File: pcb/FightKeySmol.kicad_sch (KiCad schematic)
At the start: 31 parts, among them J1 Conn_01x08_Male, J2 Conn_01x08_Male, U1 Pico

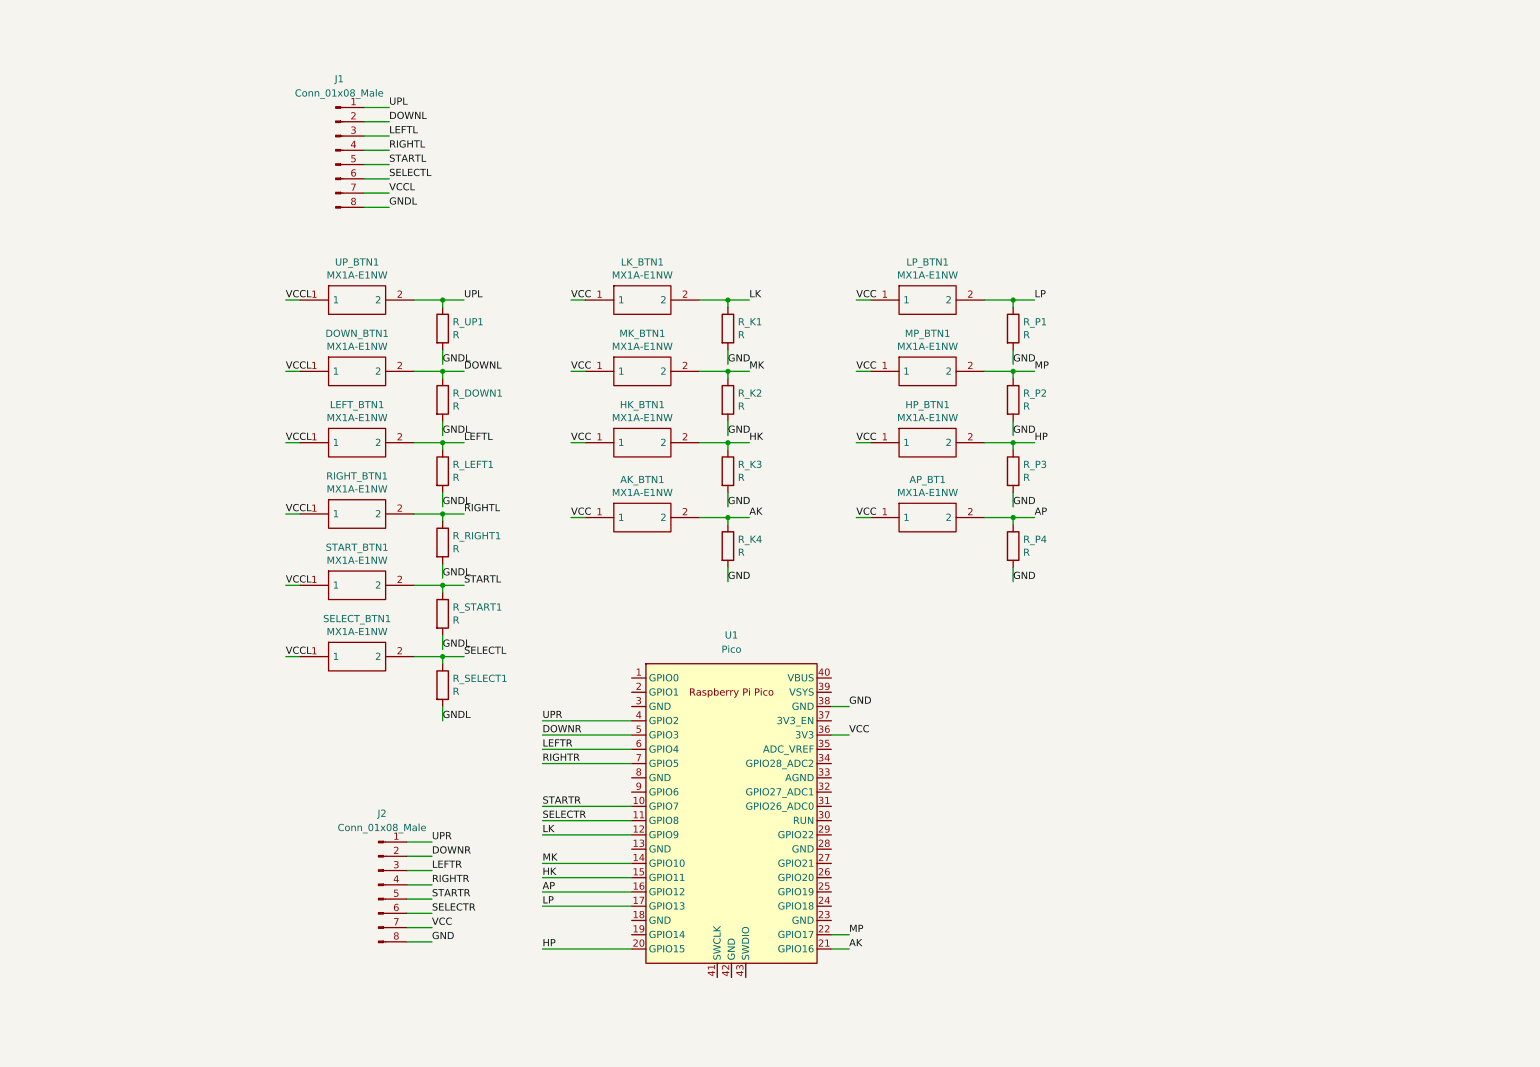
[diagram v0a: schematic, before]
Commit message: kicad_sch: redesigned to use input_pullup
This is the standard for GP2040 style sticks.
Use PICO_BOARD_CONFIG_H_

Signed-off-by: Dylan Turner <dylantdmt@gmail.com>
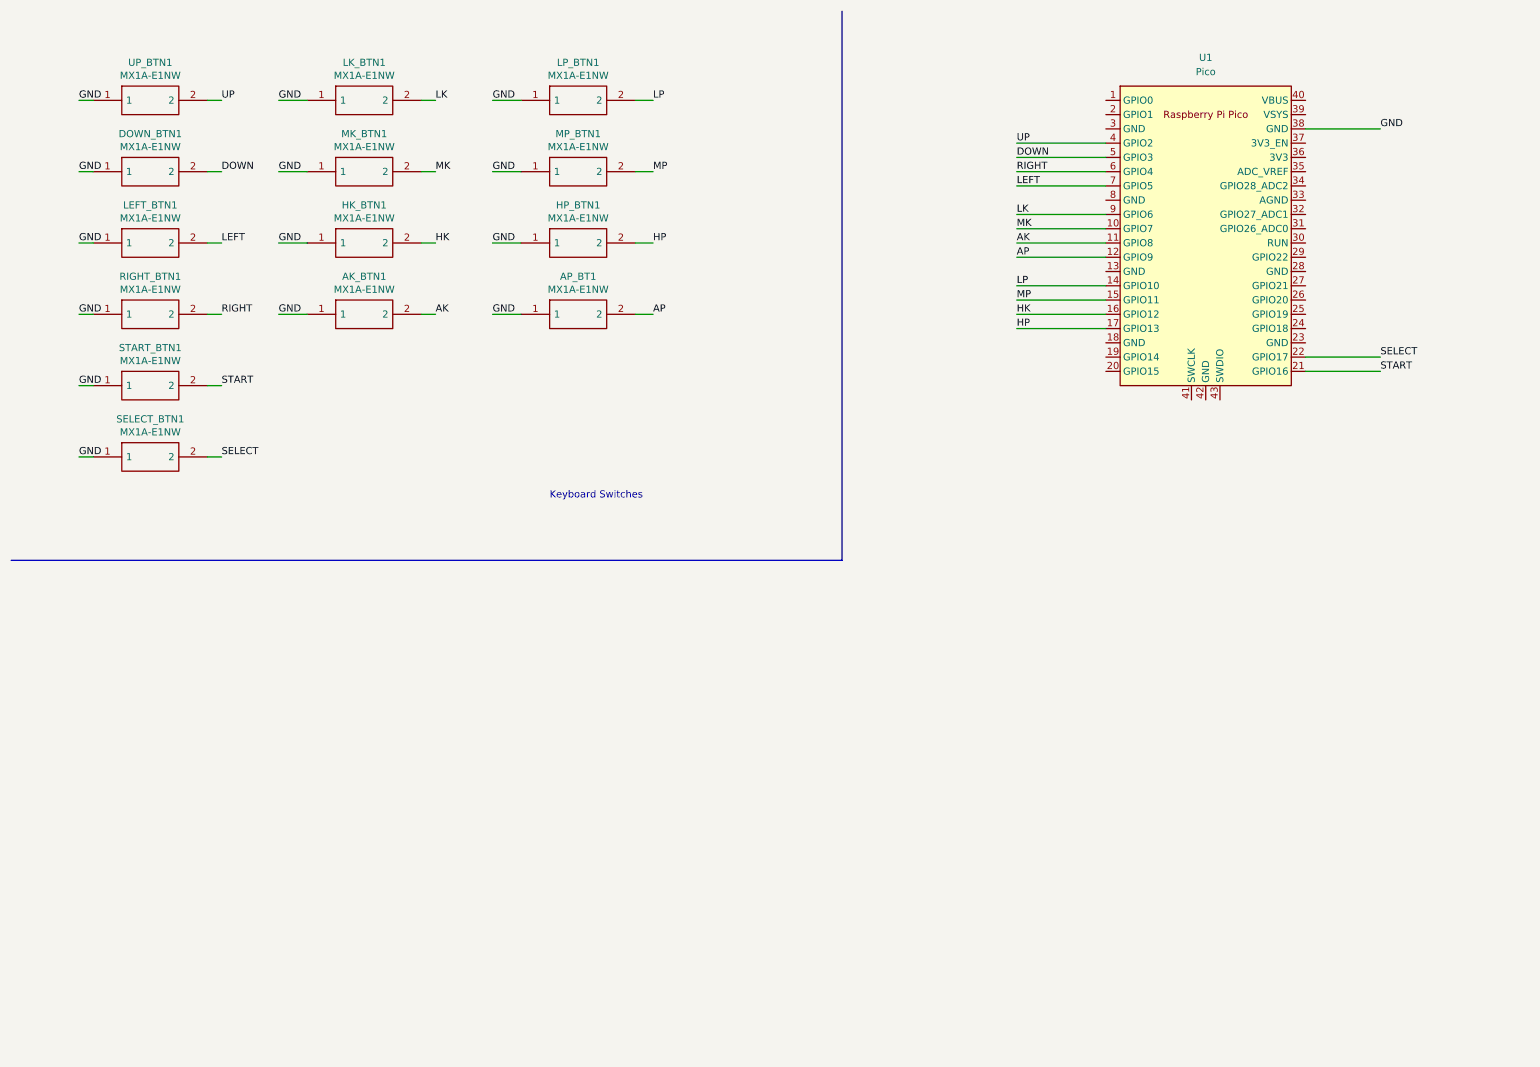
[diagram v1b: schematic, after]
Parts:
- removed J1, J2: Conn_01x08_Male, Connector_PinHeader_2.54mm:PinHeader_1x08_P2.54mm_Vertical, symbol Connector:Conn_01x08_Male
- removed R_DOWN1, R_K1, R_K2, R_K3, R_K4, R_LEFT1, R_P1, R_P2, R_P3, R_P4, R_RIGHT1, R_SELECT1, R_START1, R_UP1: R, Resistor_THT:R_Axial_DIN0204_L3.6mm_D1.6mm_P2.54mm_Vertical, symbol Device:R
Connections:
- net DOWNR is gone; now on net DOWN: U1.5 (GPIO3)
- net RIGHTL is gone; now on net RIGHT: RIGHT_BTN1.2
- net RIGHTR is gone; now on net LEFT: U1.7 (GPIO5)
- net SELECTR is gone; now on net AK: U1.11 (GPIO8)
- net STARTR is gone; now on net MK: U1.10 (GPIO7)
- net UPR is gone; now on net UP: U1.4 (GPIO2)
- net VCCL is gone; now on net GND: DOWN_BTN1.1, LEFT_BTN1.1, RIGHT_BTN1.1, SELECT_BTN1.1, START_BTN1.1, UP_BTN1.1
- net AK: no longer U1.21 (GPIO16)
- net AP: now also U1.12 (GPIO9); no longer U1.16 (GPIO12)
- net GND: now also AK_BTN1.1, AP_BT1.1, HK_BTN1.1, HP_BTN1.1, LK_BTN1.1, LP_BTN1.1, MK_BTN1.1, MP_BTN1.1
- net HK: now also U1.16 (GPIO12); no longer U1.15 (GPIO11)
- net HP: now also U1.17 (GPIO13); no longer U1.20 (GPIO15)
- net LK: now also U1.9 (GPIO6); no longer U1.12 (GPIO9)
- net LP: now also U1.14 (GPIO10); no longer U1.17 (GPIO13)
- net MK: no longer U1.14 (GPIO10)
- net MP: now also U1.15 (GPIO11); no longer U1.22 (GPIO17)
- net DOWNL renamed DOWN
- net LEFTL renamed LEFT
- net LEFTR renamed RIGHT
- net SELECTL renamed SELECT
- net SELECT: now also U1.22 (GPIO17)
- net STARTL renamed START
- net START: now also U1.21 (GPIO16)
- net UPL renamed UP
- removed net VCC: AK_BTN1.1, AP_BT1.1, HK_BTN1.1, HP_BTN1.1, LK_BTN1.1, LP_BTN1.1, MK_BTN1.1, MP_BTN1.1, U1.36 (3V3)
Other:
- note added: "Keyboard Switches"
- moved on the sheet: AK_BTN1, AP_BT1, DOWN_BTN1, HK_BTN1, HP_BTN1, LEFT_BTN1, LK_BTN1, LP_BTN1, MK_BTN1, MP_BTN1, RIGHT_BTN1, SELECT_BTN1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

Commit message: kicad_sch: added second ground on other side
Signed-off-by: Dylan Turner <dylantdmt@gmail.com>
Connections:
- net GND: now also U1.3 (GND)
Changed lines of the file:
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@@
+    (stroke (width 0) (type default) (color 0 0 0 0))
+  )
+  (wire (pts (xy 191.135 33.02) (xy 207.01 33.02))
     (stroke (width 0) (type default) (color 0 0 0 0))
   )
@@
     (effects (font (size 1.27 1.27)) (justify left bottom))
   )
+  (label "GND" (at 191.135 33.02 0)
+    (effects (font (size 1.27 1.27)) (justify left bottom))
+  )

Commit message: kicad_sch: switch start/sel
Signed-off-by: Dylan Turner <dylantdmt@gmail.com>
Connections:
- net SELECT: now also U1.21 (GPIO16); no longer U1.22 (GPIO17)
- net START: now also U1.22 (GPIO17); no longer U1.21 (GPIO16)
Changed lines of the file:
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@@
-    (effects (font (size 1.27 1.27)) (justify left bottom))
-  )
-  (label "SELECT" (at 255.905 73.66 0)
     (effects (font (size 1.27 1.27)) (justify left bottom))
   )
@@
   )
   (label "GND" (at 97.79 40.64 0)
+    (effects (font (size 1.27 1.27)) (justify left bottom))
+  )
+  (label "SELECT" (at 255.905 76.2 0)
     (effects (font (size 1.27 1.27)) (justify left bottom))
   )
@@
     (effects (font (size 1.27 1.27)) (justify left bottom))
   )
-  (label "START" (at 255.905 76.2 0)
-    (effects (font (size 1.27 1.27)) (justify left bottom))
-  )
   (label "UP" (at 49.53 27.94 0)
     (effects (font (size 1.27 1.27)) (justify left bottom))
@@
     (effects (font (size 1.27 1.27)) (justify left bottom))
   )
+  (label "START" (at 255.905 73.66 0)
+    (effects (font (size 1.27 1.27)) (justify left bottom))
+  )

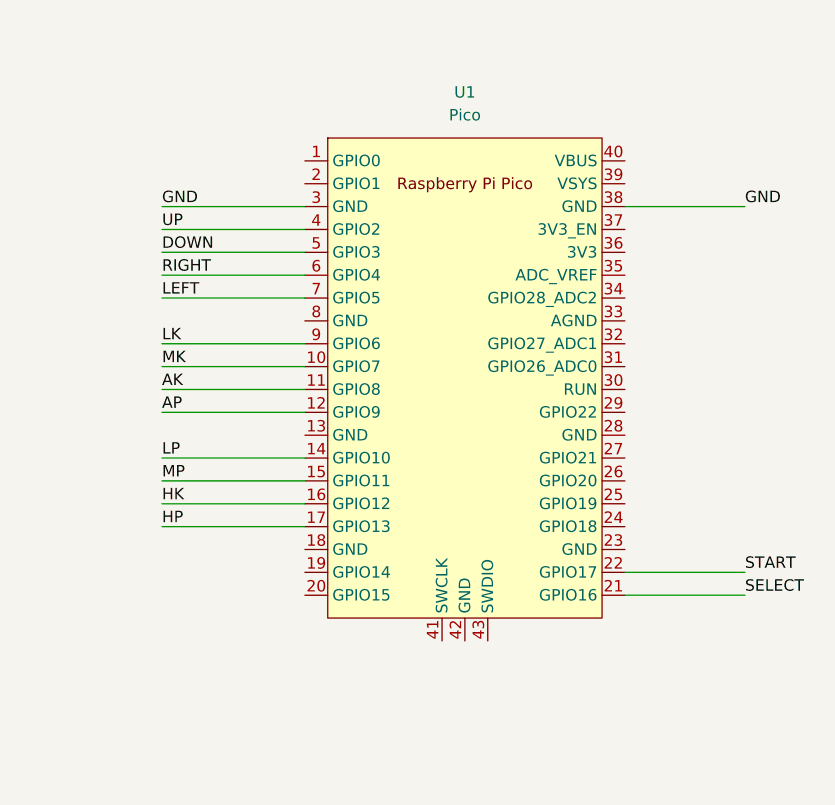
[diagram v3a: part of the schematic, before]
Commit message: kicad_sch: delete pico
Signed-off-by: Dylan Turner <dylantdmt@gmail.com>
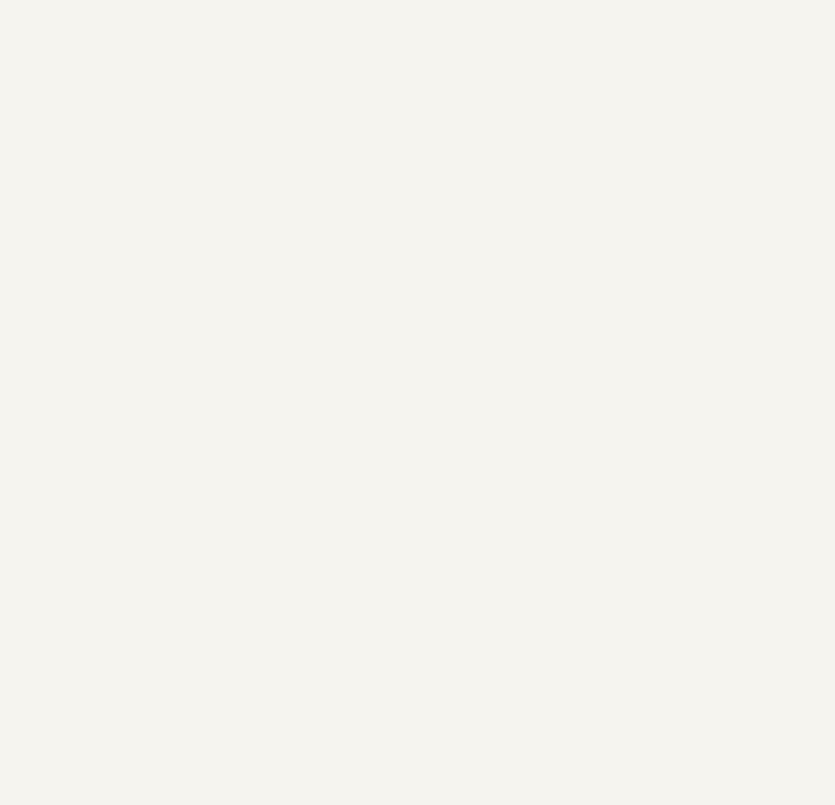
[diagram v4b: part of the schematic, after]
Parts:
- removed U1: Pico, MCU_RaspberryPi_and_Boards:RPi_Pico_SMD_TH, symbol MCU_RaspberryPi_and_Boards:Pico
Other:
- title: Fight Key PCB -> Fight Key Smol PCB
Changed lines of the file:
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@@
   (paper "A4")
   (title_block
-    (title "Fight Key PCB")
-    (date "2022-05-21")
+    (title "Fight Key Smol PCB")
+    (date "2023-04-14")
     (rev "2")
     (company "Dylan Turner")
@@
     (stroke (width 0) (type default) (color 0 0 0 0))
   )
-  (wire (pts (xy 191.135 68.58) (xy 207.01 68.58))
-    (stroke (width 0) (type default) (color 0 0 0 0))
-  )
   (wire (pts (xy 46.99 53.34) (xy 49.53 53.34))
     (stroke (width 0) (type default) (color 0 0 0 0))
   )
-  (wire (pts (xy 191.135 43.18) (xy 207.01 43.18))
-    (stroke (width 0) (type default) (color 0 0 0 0))
-  )
   (wire (pts (xy 26.67 91.44) (xy 24.13 91.44))
     (stroke (width 0) (type default) (color 0 0 0 0))
@@
     (stroke (width 0) (type default) (color 0 0 0 0))
   )
-  (wire (pts (xy 242.57 73.66) (xy 255.905 73.66))
-    (stroke (width 0) (type default) (color 0 0 0 0))
-  )
-  (wire (pts (xy 191.135 55.88) (xy 207.01 55.88))
-    (stroke (width 0) (type default) (color 0 0 0 0))
-  )
-  (wire (pts (xy 191.135 33.02) (xy 207.01 33.02))
-    (stroke (width 0) (type default) (color 0 0 0 0))
-  )
-  (wire (pts (xy 191.135 38.1) (xy 207.01 38.1))
-    (stroke (width 0) (type default) (color 0 0 0 0))
-  )
   (wire (pts (xy 85.09 66.04) (xy 87.63 66.04))
     (stroke (width 0) (type default) (color 0 0 0 0))
@@
     (stroke (width 0) (type default) (color 0 0 0 0))
   )
-  (wire (pts (xy 242.57 33.02) (xy 255.905 33.02))
-    (stroke (width 0) (type default) (color 0 0 0 0))
-  )
   (wire (pts (xy 26.67 40.64) (xy 24.13 40.64))
     (stroke (width 0) (type default) (color 0 0 0 0))
@@
     (stroke (width 0) (type default) (color 0 0 0 0))
   )
-  (wire (pts (xy 191.135 50.8) (xy 207.01 50.8))
-    (stroke (width 0) (type default) (color 0 0 0 0))
-  )
-  (wire (pts (xy 191.135 53.34) (xy 207.01 53.34))
-    (stroke (width 0) (type default) (color 0 0 0 0))
-  )
   (wire (pts (xy 85.09 40.64) (xy 87.63 40.64))
     (stroke (width 0) (type default) (color 0 0 0 0))
@@
     (stroke (width 0) (type default) (color 0 0 0 0))
   )
-  (wire (pts (xy 191.135 60.96) (xy 207.01 60.96))
-    (stroke (width 0) (type default) (color 0 0 0 0))
-  )
   (wire (pts (xy 46.99 91.44) (xy 49.53 91.44))
     (stroke (width 0) (type default) (color 0 0 0 0))
   )
-  (wire (pts (xy 191.135 48.26) (xy 207.01 48.26))
-    (stroke (width 0) (type default) (color 0 0 0 0))
-  )
   (wire (pts (xy 26.67 66.04) (xy 24.13 66.04))
     (stroke (width 0) (type default) (color 0 0 0 0))
   )
-  (wire (pts (xy 242.57 76.2) (xy 255.905 76.2))
-    (stroke (width 0) (type default) (color 0 0 0 0))
-  )
-  (wire (pts (xy 191.135 63.5) (xy 207.01 63.5))
-    (stroke (width 0) (type default) (color 0 0 0 0))
-  )
-  (wire (pts (xy 191.135 66.04) (xy 207.01 66.04))
-    (stroke (width 0) (type default) (color 0 0 0 0))
-  )
   (wire (pts (xy 46.99 78.74) (xy 49.53 78.74))
     (stroke (width 0) (type default) (color 0 0 0 0))
   )
-  (wire (pts (xy 191.135 35.56) (xy 207.01 35.56))
-    (stroke (width 0) (type default) (color 0 0 0 0))
-  )
   (wire (pts (xy 97.79 66.04) (xy 102.87 66.04))
     (stroke (width 0) (type default) (color 0 0 0 0))
@@
     (stroke (width 0) (type default) (color 0 0 0 0))
   )
-  (wire (pts (xy 191.135 40.64) (xy 207.01 40.64))
-    (stroke (width 0) (type default) (color 0 0 0 0))
-  )
   (wire (pts (xy 123.19 66.04) (xy 126.365 66.04))
     (stroke (width 0) (type default) (color 0 0 0 0))
@@
     (effects (font (size 1.27 1.27)) (justify left bottom))
   )
-  (label "GND" (at 255.905 33.02 0)
-    (effects (font (size 1.27 1.27)) (justify left bottom))
-  )
   (label "GND" (at 97.79 27.94 0)
     (effects (font (size 1.27 1.27)) (justify left bottom))
   )
-  (label "GND" (at 191.135 33.02 0)
-    (effects (font (size 1.27 1.27)) (justify left bottom))
-  )
   (label "GND" (at 24.13 66.04 0)
     (effects (font (size 1.27 1.27)) (justify left bottom))
   )
-  (label "RIGHT" (at 191.135 40.64 0)
-    (effects (font (size 1.27 1.27)) (justify left bottom))
-  )
   (label "DOWN" (at 49.53 40.64 0)
     (effects (font (size 1.27 1.27)) (justify left bottom))
@@
     (effects (font (size 1.27 1.27)) (justify left bottom))
   )
-  (label "SELECT" (at 255.905 76.2 0)
-    (effects (font (size 1.27 1.27)) (justify left bottom))
-  )
   (label "GND" (at 97.79 53.34 0)
     (effects (font (size 1.27 1.27)) (justify left bottom))
@@
     (effects (font (size 1.27 1.27)) (justify left bottom))
   )
-  (label "AK" (at 191.135 53.34 0)
-    (effects (font (size 1.27 1.27)) (justify left bottom))
-  )
   (label "START" (at 49.53 78.74 0)
     (effects (font (size 1.27 1.27)) (justify left bottom))
   )
-  (label "MP" (at 191.135 63.5 0)
-    (effects (font (size 1.27 1.27)) (justify left bottom))
-  )
-  (label "DOWN" (at 191.135 38.1 0)
-    (effects (font (size 1.27 1.27)) (justify left bottom))
-  )
   (label "GND" (at 59.69 27.94 0)
     (effects (font (size 1.27 1.27)) (justify left bottom))
@@
     (effects (font (size 1.27 1.27)) (justify left bottom))
   )
-  (label "LP" (at 191.135 60.96 0)
-    (effects (font (size 1.27 1.27)) (justify left bottom))
-  )
-  (label "HK" (at 191.135 66.04 0)
-    (effects (font (size 1.27 1.27)) (justify left bottom))
-  )
   (label "SELECT" (at 49.53 91.44 0)
     (effects (font (size 1.27 1.27)) (justify left bottom))
   )
-  (label "AP" (at 191.135 55.88 0)
-    (effects (font (size 1.27 1.27)) (justify left bottom))
-  )
   (label "HK" (at 87.63 53.34 0)
     (effects (font (size 1.27 1.27)) (justify left bottom))
@@
     (effects (font (size 1.27 1.27)) (justify left bottom))
   )
-  (label "UP" (at 191.135 35.56 0)
-    (effects (font (size 1.27 1.27)) (justify left bottom))
-  )
-  (label "START" (at 255.905 73.66 0)
-    (effects (font (size 1.27 1.27)) (justify left bottom))
-  )
   (label "GND" (at 59.69 53.34 0)
     (effects (font (size 1.27 1.27)) (justify left bottom))
   )
-  (label "HP" (at 191.135 68.58 0)
-    (effects (font (size 1.27 1.27)) (justify left bottom))
-  )
   (label "GND" (at 24.13 27.94 0)
     (effects (font (size 1.27 1.27)) (justify left bottom))
@@
   )
   (label "LEFT" (at 49.53 53.34 0)
-    (effects (font (size 1.27 1.27)) (justify left bottom))
-  )
-  (label "MK" (at 191.135 50.8 0)
-    (effects (font (size 1.27 1.27)) (justify left bottom))
-  )
-  (label "LEFT" (at 191.135 43.18 0)
-    (effects (font (size 1.27 1.27)) (justify left bottom))
-  )
-  (label "LK" (at 191.135 48.26 0)
     (effects (font (size 1.27 1.27)) (justify left bottom))
   )
@@
     (pin "2")
   )
-  (symbol (lib_id "MCU_RaspberryPi_and_Boards:Pico") (at 224.79 52.07 0) (unit 1)
-    (in_bom yes) (on_board yes) (fields_autoplaced)
-    (property "Reference" "U1" (id 0) (at 224.79 20.32 0))
-    (property "Value" "Pico" (id 1) (at 224.79 22.86 0))
-    (property "Footprint" "MCU_RaspberryPi_and_Boards:RPi_Pico_SMD_TH" (id 2) (at 224.79 52.07 90)
-      (effects (font (size 1.27 1.27)) hide)
-    )
-    (property "Datasheet" "" (id 3) (at 224.79 52.07 0)
-      (effects (font (size 1.27 1.27)) hide)
-    )
-    (pin "1")
-    (pin "10")
-    (pin "11")
-    (pin "12")
-    (pin "13")
-    (pin "14")
-    (pin "15")
-    (pin "16")
-    (pin "17")
-    (pin "18")
-    (pin "19")
-    (pin "2")
-    (pin "20")
-    (pin "21")
-    (pin "22")
-    (pin "23")
-    (pin "24")
-    (pin "25")
-    (pin "26")
-    (pin "27")
-    (pin "28")
-    (pin "29")
-    (pin "3")
-    (pin "30")
-    (pin "31")
-    (pin "32")
-    (pin "33")
-    (pin "34")
-    (pin "35")
-    (pin "36")
-    (pin "37")
-    (pin "38")
-    (pin "39")
-    (pin "4")
-    (pin "40")
-    (pin "41")
-    (pin "42")
-    (pin "43")
-    (pin "5")
-    (pin "6")
-    (pin "7")
-    (pin "8")
-    (pin "9")
-  )
   (sheet_instances
     (path "/" (page "1"))
@@
       (reference "START_BTN1") (unit 1) (value "MX1A-E1NW") (footprint "MX1AE1NW")
     )
-    (path "/d4e6700a-2b65-4011-8d11-4ac8dc105563"
-      (reference "U1") (unit 1) (value "Pico") (footprint "MCU_RaspberryPi_and_Boards:RPi_Pico_SMD_TH")
-    )
     (path "/00000000-0000-0000-0000-0000614a626a"
